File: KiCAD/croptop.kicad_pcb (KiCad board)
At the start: 4 copper layers, 115.6 x 45.7 mm, 242 parts, among them J1 PICKit Header, J2 USB_A, J3 5V USB, J4 4-1734839-0, J5 Terminal Block, J6 DNP, J7 DNP, SW1 BTNA, SW2 BTNA, U1 PIC32MX795F512L, U10 AD7799, U11 74HCT125D, U12 Si7006-A20, U13 UCAM-M8Q, U14 W25N01GV, U15 LIS3DH, U16 PUSBM5V5X4, U17 DT6250-06MR-13, U18 PUSBM5V5X4, U2 REG71055, U3 FAN5333BSX, U4 MIC23050, U5 TC1014, U6 FT812Q, U8 74HCT125D, U9 DRV8872, Y1 CXO, Y2 12MHz

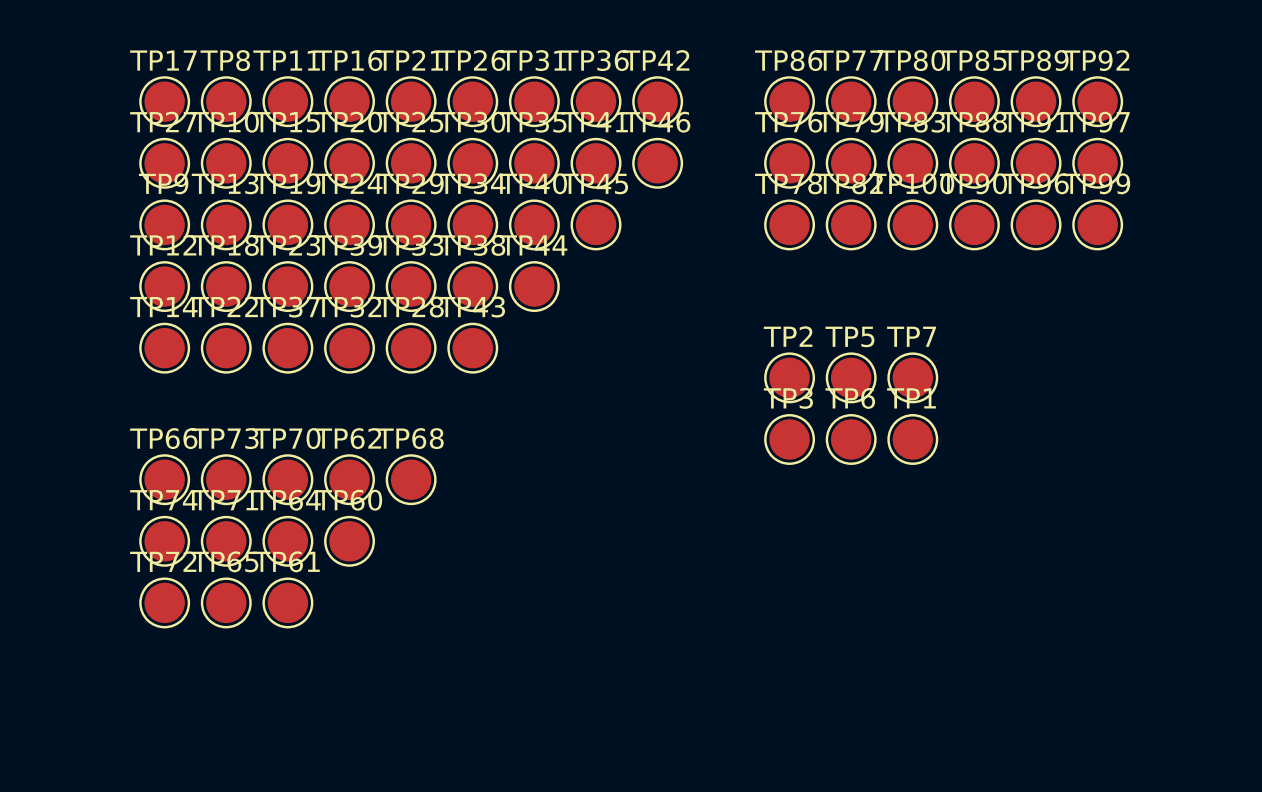
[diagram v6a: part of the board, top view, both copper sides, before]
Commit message: Changed testpoint size
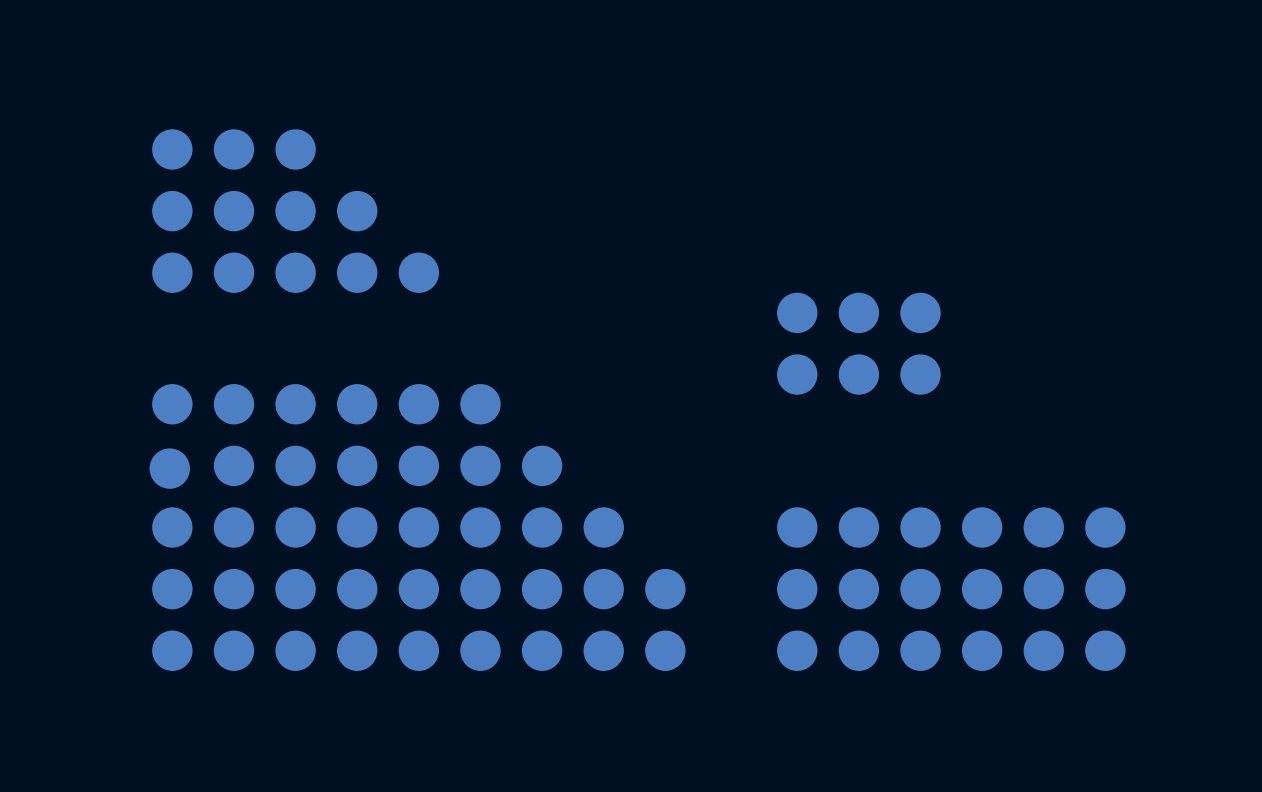
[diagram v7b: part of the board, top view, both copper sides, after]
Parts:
- TP1, TP10, TP100, TP11, TP12, TP13, TP14, TP15, TP16, TP17, TP18, TP19, TP2, TP20, TP21, TP22, TP23, TP24, TP25, TP26, TP27, TP28, TP29, TP3, TP30, TP31, TP32, TP33, TP34, TP35, TP36, TP37, TP38, TP39, TP40, TP41, TP42, TP43, TP44, TP45, TP46, TP5, TP6, TP60, TP61, TP62, TP64, TP65, TP66, TP68, TP7, TP70, TP71, TP72, TP73, TP74, TP76, TP77, TP78, TP79, TP8, TP80, TP82, TP83, TP85, TP86, TP88, TP89, TP9, TP90, TP91, TP92, TP96, TP97, TP99: moved to B.Cu
- moved TP11 27.2 mm to (105.3, 89.3)
- moved TP16 27.2 mm to (108.3, 89.3)
- moved TP17 27.2 mm to (99.2, 89.3)
- moved TP21 27.2 mm to (111.4, 89.3)
- moved TP26 27.2 mm to (114.4, 89.3)
- moved TP31 27.2 mm to (117.5, 89.3)
- moved TP36 27.2 mm to (120.5, 89.3)
- moved TP42 27.2 mm to (123.6, 89.3)
- moved TP77 27.2 mm to (133.2, 89.3)
- moved TP8 27.2 mm to (102.2, 89.3)
- moved TP80 27.2 mm to (136.2, 89.3)
- moved TP85 27.2 mm to (139.3, 89.3)
- moved TP86 27.2 mm to (130.1, 89.3)
- moved TP89 27.2 mm to (142.3, 89.3)
- moved TP92 27.2 mm to (145.4, 89.3)
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
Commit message: Complete PCB version 1
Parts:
- removed TP76, TP77, TP79, TP80, TP96, TP97: TestPoint_Alt, TestPoint:TestPoint_Pad_D2.0mm
- added G***: LOGO, croptop:croptoplogo, F.Cu at (136.5, 107.4)
- added G***: LOGO, croptop:usblogo, F.Cu at (164.0, 101.3)
- added G***: LOGO, croptop:touch, F.Cu at (145.7, 138.0)
- added G***: LOGO, croptop:gnss, F.Cu at (85.1, 103.3)
- added G***: LOGO, croptop:idaho, B.Cu at (134.7, 103.6)
- TP1, TP10, TP100, TP11, TP12, TP13, TP14, TP15, TP16, TP17, TP18, TP19, TP2, TP20, TP21, TP22, TP23, TP24, TP25, TP26, TP27, TP28, TP29, TP3, TP30, TP31, TP32, TP33, TP34, TP35, TP36, TP37, TP38, TP39, TP40, TP41, TP42, TP43, TP44, TP45, TP46, TP5, TP6, TP60, TP61, TP62, TP64, TP65, TP66, TP68, TP7, TP70, TP71, TP72, TP73, TP74, TP78, TP8, TP82, TP83, TP85, TP86, TP88, TP89, TP9, TP90, TP91, TP92, TP99: footprint TestPoint:TestPoint_Pad_D2.0mm -> croptop:TestPoint
- moved TP37 78.2 mm to (156.8, 135.9)
- moved TP3 77.7 mm to (82.9, 134.3)
- moved TP39 75.6 mm to (159.4, 135.9)
- moved TP72 72.4 mm to (79.6, 134.2)
- moved TP32 71.8 mm to (154.8, 131.8)
- moved TP38 71.2 mm to (158.1, 136.4)
- moved TP22 69.4 mm to (145.0, 131.8)
- moved TP27 69.4 mm to (149.9, 133.5)
- moved TP33 69.4 mm to (155.6, 133.6)
- moved TP40 67.7 mm to (160.5, 135.4)
- moved TP28 67.5 mm to (150.9, 131.8)
- moved TP71 67.5 mm to (91.8, 134.2)
- moved TP23 67.1 mm to (145.9, 133.5)
- moved TP14 66.5 mm to (137.0, 131.8)
- moved TP70 66.2 mm to (87.6, 134.3)
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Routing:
- net BTN_B: track 48.6 -> 69.8 mm, vias 2 -> 3
- net BTN_A: track 57.6 -> 74.5 mm, vias 2 -> 3
- net TCH_DOWN: track 31.5 -> 37.1 mm
- net TCH_RIGHT: track 30.4 -> 35.2 mm
- net NAND_CS: track 27.6 -> 32.2 mm
- net TCH_LEFT: track 32.5 -> 37.1 mm
- net DRV_GND: track 260.9 -> 265.4 mm, vias 91 -> 92
- net ADC_A1-: track 11.3 -> 15.7 mm
- net DRV_IN2: track 39.5 -> 43.7 mm
- net ADC_A1+: track 10.2 -> 14.2 mm
- net LIN_IN: track 26.4 -> 30.0 mm
- net SCL: track 64.4 -> 68.0 mm
- net DVDD_UNREG: track 116.2 -> 119.4 mm
- net TCH_UP: track 33.5 -> 36.6 mm
- net RX: track 21.3 -> 24.4 mm
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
